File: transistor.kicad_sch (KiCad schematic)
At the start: 5 parts, among them J9 Conn_01x02_Pin, Q1 AO3400A

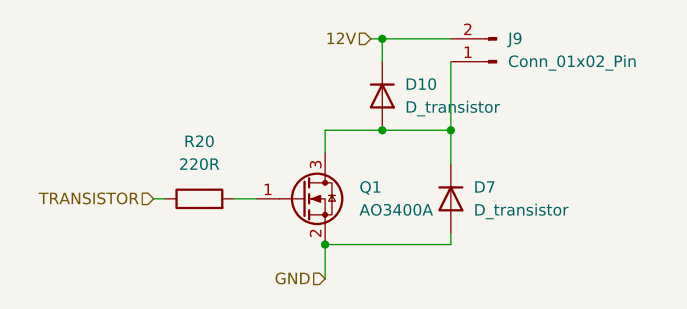
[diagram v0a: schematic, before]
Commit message: update to Kicad 10 + fix warnings
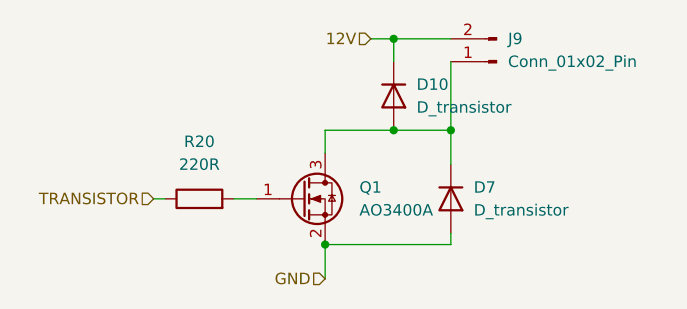
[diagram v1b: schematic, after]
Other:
- moved on the sheet: D10
